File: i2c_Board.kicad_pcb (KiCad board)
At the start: 2 copper layers, 29.5 x 39.2 mm, 23 parts, among them J1 Conn_01x09_Pin, J2 Logic Analyzer Connector Pins, U1 MCP9808, U2 MCP7940N, Y1 Crystal

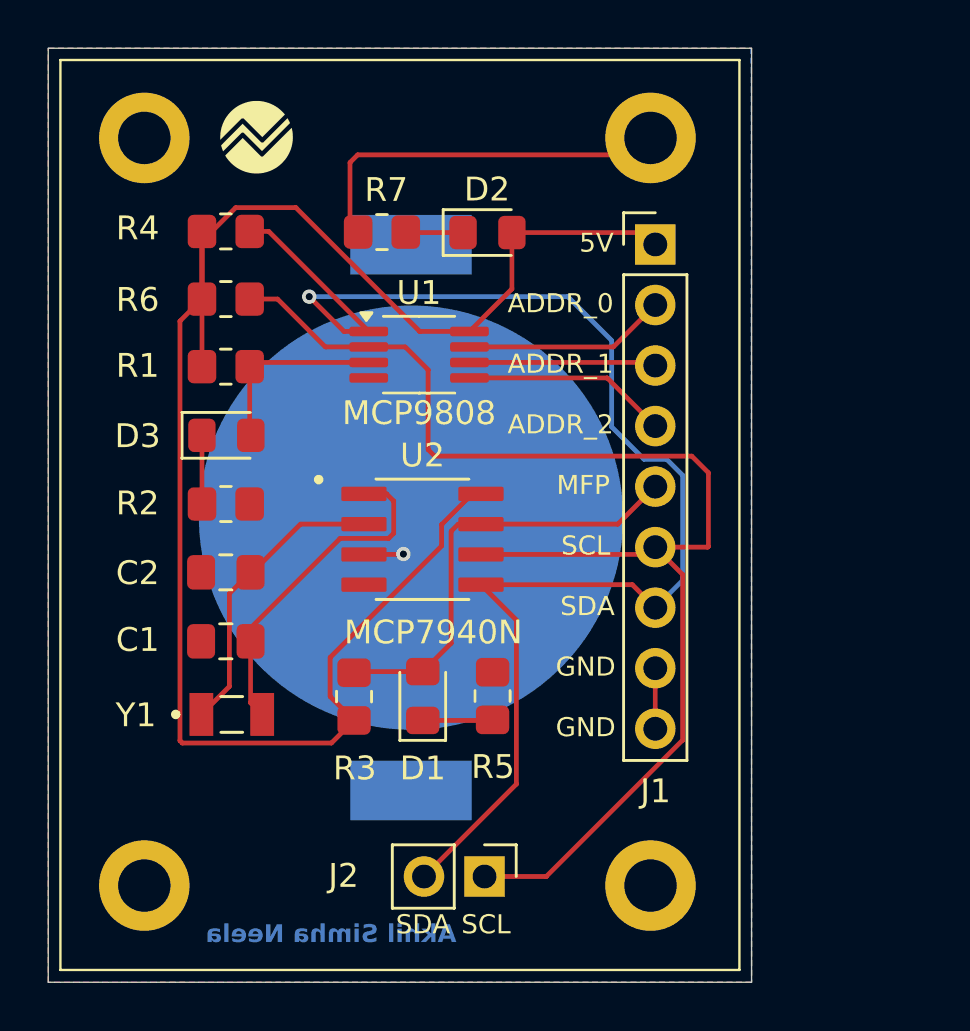
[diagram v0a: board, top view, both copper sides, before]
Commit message: Moved battery holder position
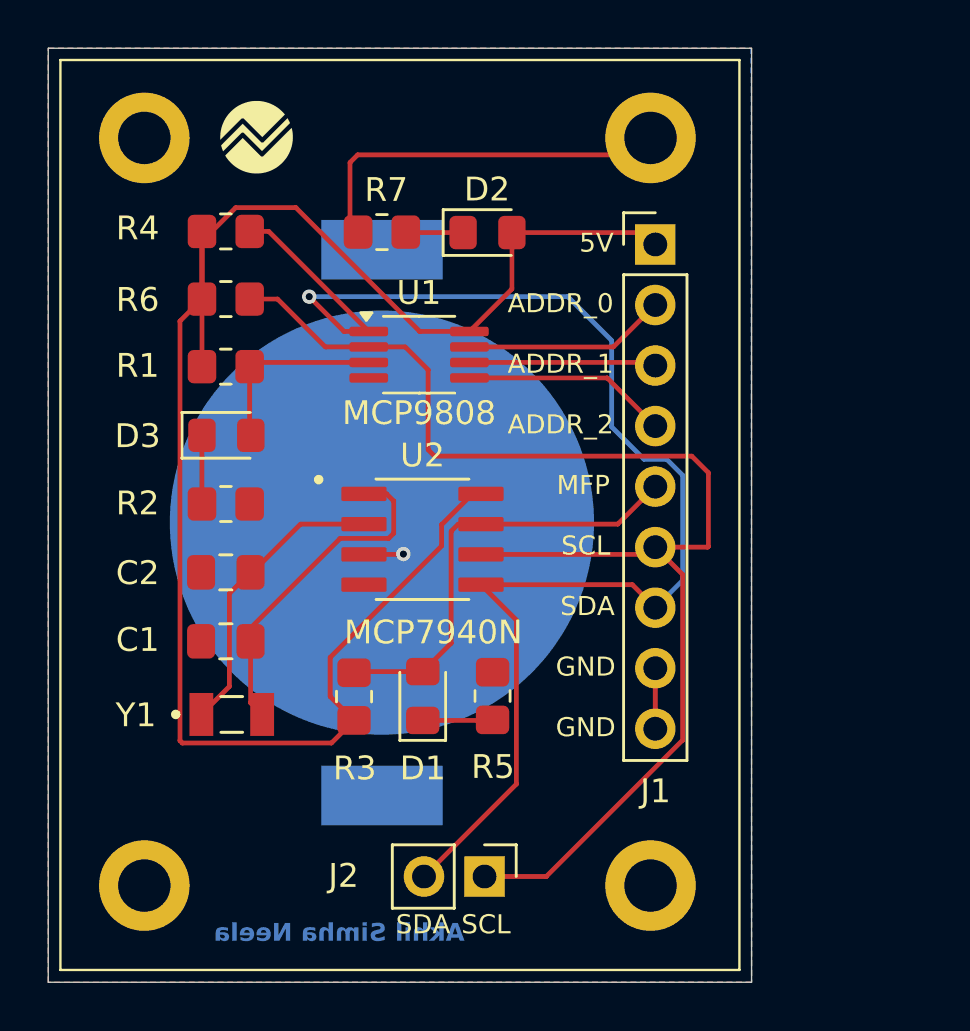
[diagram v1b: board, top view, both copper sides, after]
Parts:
- moved BT1 1.24 mm to (151.7, 92.1)
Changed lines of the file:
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@@
 	(footprint "BAT-HLD-002-SMT:BAT_BAT-HLD-002-SMT"
 		(layer "B.Cu")
-		(at 152.94 91.89 90)
+		(at 151.72 92.1 90)
 		(property "Reference" "BT1"
-			(at -11.82 -6.66 0)
+			(at 11.66 5.96 0)
 			(layer "B.SilkS")
 			(effects
@@
 	)
 	(gr_text "Akhil Simha Neela"
-		(at 154.85 109.79 -0)
+		(at 155.19 109.74 -0)
 		(layer "B.Cu")
 		(effects
@@
 	)
 	(gr_text "v 1.1"
-		(at 142.6 100.73 90)
+		(at 142.58 98.66 90)
 		(layer "B.SilkS")
 		(effects
 			(font
 				(size 1 1)
-				(thickness 0.2)
+				(thickness 0.125)
 				(bold yes)
 			)
@@
 	)
 	(gr_text "I2C Learning Board"
-		(at 142.59 78.16 90)
+		(at 141.09 80.58 90)
 		(layer "B.SilkS")
 		(effects

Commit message: Added Decoupling Capacitors
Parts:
- added C3: 0.1u, Capacitor_SMD:C_0805_2012Metric_Pad1.18x1.45mm_HandSolder, F.Cu at (159.1, 82.6)
- added C4: 0.1u, Capacitor_SMD:C_0805_2012Metric_Pad1.18x1.45mm_HandSolder, F.Cu at (159.6, 90.7)
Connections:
- U1 pad 8: +5V -> Net-(U1-V_{DD})
- U2 pad 8: +5V -> Net-(U2-VCC)
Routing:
- net GND: track 18.7 -> 45.8 mm, vias 0 -> 2
- net +5V: track 72.6 -> 81.3 mm
- net Net-(U1-V_{DD}): track 0.00 -> 3.89 mm
- net Net-(U2-VCC): track 0.00 -> 2.78 mm

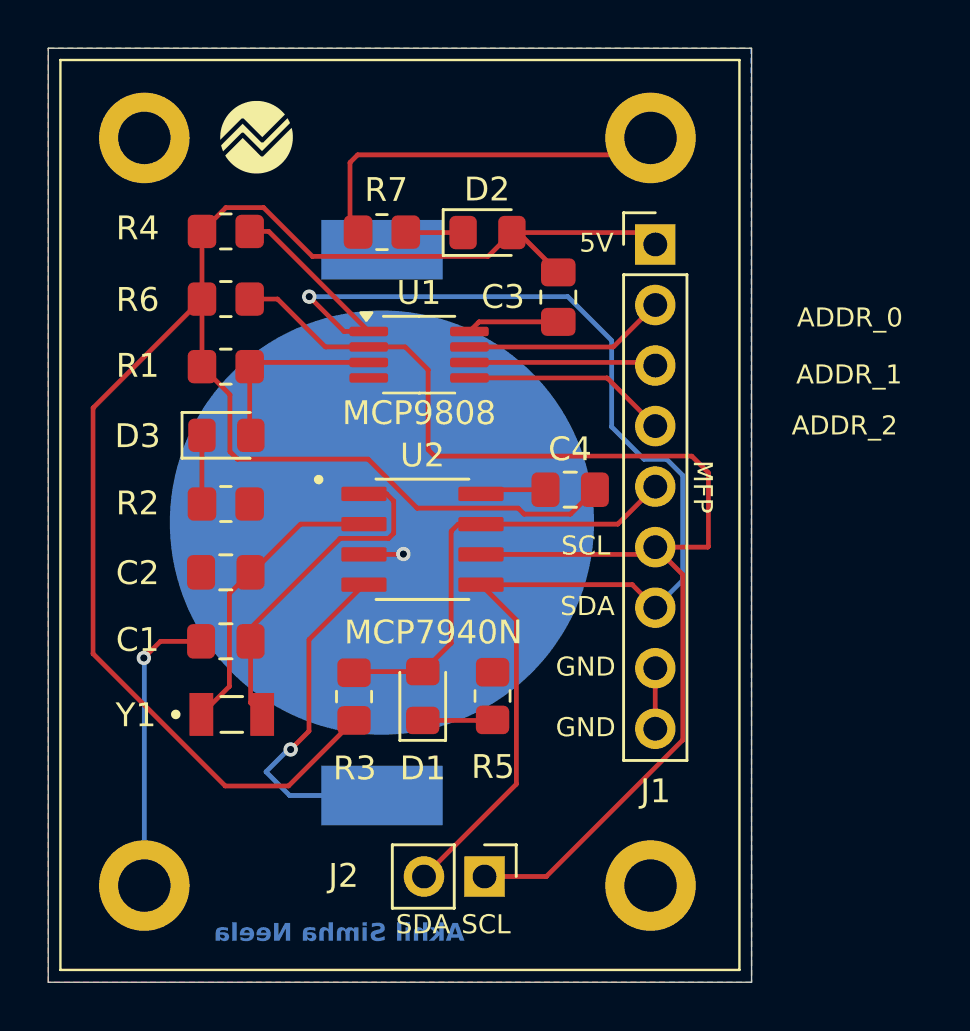
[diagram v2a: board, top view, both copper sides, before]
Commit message: Flipped incorrect battery polarity
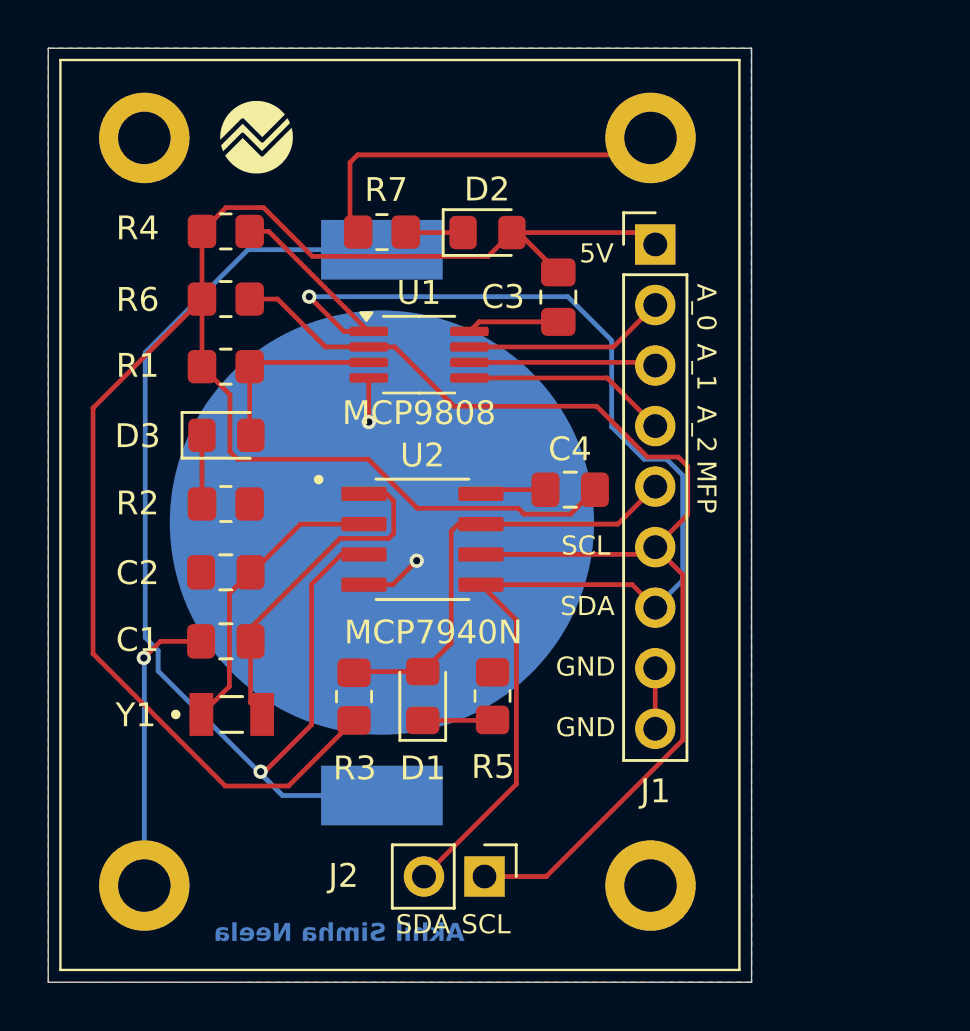
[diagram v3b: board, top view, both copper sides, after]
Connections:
- BT1 pad N: Net-(U2-VBAT) -> GND
- BT1 pad P1: GND -> Net-(U2-VBAT)
- BT1 pad P2: GND -> Net-(U2-VBAT)
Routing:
- net Net-(U2-VBAT): track 1.66 -> 49.8 mm
- net GND: track 45.8 -> 35.4 mm, vias 2 -> 3
- net MCU_SCL: track 56.3 -> 51.9 mm
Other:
- board text added: "A_0"
- board text added: "A_1"
- board text added: "A_2"
- board text removed: "ADDR_0"
- board text removed: "ADDR_1"
- board text removed: "ADDR_2"
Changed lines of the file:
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@@
 			(size 17.8 17.8)
 			(layers "B.Cu" "B.Mask")
-			(net 15 "Net-(U2-VBAT)")
+			(net 1 "GND")
 			(pintype "passive")
 			(solder_mask_margin 0.102)
@@
 			(size 2.5 5.1)
 			(layers "B.Cu" "B.Paste" "B.Mask")
-			(net 1 "GND")
+			(net 15 "Net-(U2-VBAT)")
 			(pintype "passive")
 			(solder_mask_margin 0.102)
@@
 			(size 2.5 5.1)
 			(layers "B.Cu" "B.Paste" "B.Mask")
-			(net 1 "GND")
+			(net 15 "Net-(U2-VBAT)")
 			(pintype "passive")
 			(solder_mask_margin 0.102)
@@
 		)
 	)
-	(gr_text "ADDR_0"
-		(at 169.13 83.97 0)
+	(gr_text "A_0"
+		(at 164.86 82.07 -90)
 		(layer "F.SilkS")
 		(effects
@@
 		)
 	)
-	(gr_text "ADDR_1"
-		(at 169.1 86.36 0)
+	(gr_text "A_1"
+		(at 164.86 84.58 -90)
 		(layer "F.SilkS")
 		(effects
@@
 	)
 	(gr_text "MFP"
-		(at 164.71 89.48 -90)
+		(at 164.86 89.48 -90)
 		(layer "F.SilkS")
 		(effects
@@
 	)
 	(gr_text "5V"
-		(at 160.000476 80.83 0)
+		(at 160.000476 81.28 0)
 		(layer "F.SilkS")
 		(effects
@@
 		)
 	)
-	(gr_text "ADDR_2"
-		(at 168.91 88.5 0)
+	(gr_text "A_2"
+		(at 164.86 87.18 -90)
 		(layer "F.SilkS")
 		(effects
@@
 	)
 	(segment
+		(start 152.175 94.705)
+		(end 153.18 93.7)
+		(width 0.2)
+		(layer "F.Cu")
+		(net 1)
+	)
+	(segment
+		(start 150.965 94.705)
+		(end 152.175 94.705)
+		(width 0.2)
+		(layer "F.Cu")
+		(net 1)
+	)
+	(segment
 		(start 141.73 97.78)
 		(end 142.427144 97.082856)
@@
 	)
 	(segment
+		(start 151.1675 86.03)
+		(end 151.1675 87.8775)
+		(width 0.2)
+		(layer "F.Cu")
+		(net 1)
+	)
+	(segment
 		(start 142.427144 97.082856)
 		(end 144.1325 97.082856)
@@
 	)
 	(segment
-		(start 148.66 100.85)
-		(end 148.66 97.01)
+		(start 151.1675 87.8775)
+		(end 151.17 87.88)
 		(width 0.2)
 		(layer "F.Cu")
@@
 		(net 1)
 	)
-	(segment
-		(start 148.66 97.01)
-		(end 150.965 94.705)
-		(width 0.2)
-		(layer "F.Cu")
-		(net 1)
-	)
-	(segment
-		(start 147.89 101.62)
-		(end 148.66 100.85)
-		(width 0.2)
-		(layer "F.Cu")
+	(via
+		(at 151.17 87.88)
+		(size 0.6)
+		(drill 0.3)
+		(layers "F.Cu" "B.Cu")
 		(net 1)
 	)
@@
 	)
 	(via
-		(at 147.89 101.62)
+		(at 153.18 93.7)
 		(size 0.6)
 		(drill 0.3)
@@
 	)
 	(segment
-		(start 147.89 101.62)
-		(end 147.79 101.62)
-		(width 0.2)
-		(layer "B.Cu")
-		(net 1)
-	)
-	(segment
 		(start 141.73 97.78)
 		(end 141.75 97.8)
@@
 	)
 	(segment
-		(start 146.86 102.56)
-		(end 147.85 103.55)
-		(width 0.2)
-		(layer "B.Cu")
-		(net 1)
-	)
-	(segment
-		(start 147.79 101.62)
-		(end 146.86 102.55)
-		(width 0.2)
-		(layer "B.Cu")
-		(net 1)
-	)
-	(segment
-		(start 147.85 103.55)
-		(end 151.72 103.55)
-		(width 0.2)
-		(layer "B.Cu")
-		(net 1)
-	)
-	(segment
-		(start 146.86 102.55)
-		(end 146.86 102.56)
-		(width 0.2)
-		(layer "B.Cu")
-		(net 1)
-	)
-	(segment
 		(start 152.215 92.54741)
 		(end 151.99741 92.765)
@@
 	)
 	(segment
+		(start 164.55 89.74)
+		(end 164.55 91.77)
+		(width 0.2)
+		(layer "F.Cu")
+		(net 11)
+	)
+	(segment
+		(start 151.1675 84.73)
+		(end 152.26 84.73)
+		(width 0.2)
+		(layer "F.Cu")
+		(net 11)
+	)
+	(segment
 		(start 163.19 93.13)
 		(end 164.34 94.28)
@@
 	)
 	(segment
-		(start 165.39 93.13)
-		(end 165.42 93.1)
+		(start 152.26 84.73)
+		(end 154.75 87.22)
 		(width 0.2)
 		(layer "F.Cu")
@@
 	)
 	(segment
-		(start 165.42 90.01)
-		(end 165.42 93.1)
-		(width 0.2)
-		(layer "F.Cu")
-		(net 11)
-	)
-	(segment
-		(start 153.93 89.31)
-		(end 164.72 89.31)
-		(width 0.2)
-		(layer "F.Cu")
-		(net 11)
-	)
-	(segment
-		(start 164.72 89.31)
-		(end 165.42 90.01)
-		(width 0.2)
-		(layer "F.Cu")
-		(net 11)
-	)
-	(segment
-		(start 153.66 85.69)
-		(end 153.66 89.04)
-		(width 0.2)
-		(layer "F.Cu")
-		(net 11)
-	)
-	(segment
 		(start 164.34 101.226346)
 		(end 158.616346 106.95)
@@
 	)
 	(segment
-		(start 153.66 89.04)
-		(end 153.93 89.31)
-		(width 0.2)
-		(layer "F.Cu")
-		(net 11)
-	)
-	(segment
 		(start 149.35 84.73)
 		(end 151.1675 84.73)
@@
 	)
 	(segment
-		(start 152.7 84.73)
-		(end 153.66 85.69)
-		(width 0.2)
-		(layer "F.Cu")
-		(net 11)
-	)
-	(segment
-		(start 151.1675 84.73)
-		(end 152.7 84.73)
+		(start 162.863654 89.35)
+		(end 164.16 89.35)
+		(width 0.2)
+		(layer "F.Cu")
+		(net 11)
+	)
+	(segment
+		(start 154.75 87.22)
+		(end 160.733654 87.22)
+		(width 0.2)
+		(layer "F.Cu")
+		(net 11)
+	)
+	(segment
+		(start 164.16 89.35)
+		(end 164.55 89.74)
 		(width 0.2)
 		(layer "F.Cu")
@@
 	)
 	(segment
-		(start 163.19 93.13)
-		(end 165.39 93.13)
+		(start 164.55 91.77)
+		(end 163.19 93.13)
 		(width 0.2)
 		(layer "F.Cu")
@@
 		(start 162.885 93.435)
 		(end 163.19 93.13)
+		(width 0.2)
+		(layer "F.Cu")
+		(net 11)
+	)
+	(segment
+		(start 160.733654 87.22)
+		(end 162.863654 89.35)
 		(width 0.2)
 		(layer "F.Cu")
@@
 	)
 	(segment
-		(start 152.62 93.42)
-		(end 152.605 93.435)
-		(width 0.2)
-		(layer "F.Cu")
-		(net 15)
-	)
-	(segment
-		(start 152.605 93.435)
+		(start 150.015001 93.435)
 		(end 150.965 93.435)
 		(width 0.2)
@@
 		(net 15)
 	)
+	(segment
+		(start 146.63 102.55)
+		(end 146.8 102.55)
+		(width 0.2)
+		(layer "F.Cu")
+		(net 15)
+	)
+	(segment
+		(start 148.77 94.680001)
+		(end 150.015001 93.435)
+		(width 0.2)
+		(layer "F.Cu")
+		(net 15)
+	)
+	(segment
+		(start 146.8 102.55)
+		(end 148.77 100.58)
+		(width 0.2)
+		(layer "F.Cu")
+		(net 15)
+	)
+	(segment
+		(start 148.77 100.58)
+		(end 148.77 94.680001)
+		(width 0.2)
+		(layer "F.Cu")
+		(net 15)
+	)
 	(via
-		(at 152.62 93.42)
+		(at 146.63 102.55)
 		(size 0.6)
 		(drill 0.3)
@@
 		(net 15)
 	)
+	(segment
+		(start 146.63 102.63)
+		(end 147.55 103.55)
+		(width 0.2)
+		(layer "B.Cu")
+		(net 15)
+	)
+	(segment
+		(start 141.79 84.96)
+		(end 141.79 96.93)
+		(width 0.2)
+		(layer "B.Cu")
+		(net 15)
+	)
+	(segment
+		(start 141.79 96.93)
+		(end 142.33 97.47)
+		(width 0.2)
+		(layer "B.Cu")
+		(net 15)
+	)
+	(segment
+		(start 146.63 102.55)
+		(end 146.63 102.63)
+		(width 0.2)
+		(layer "B.Cu")
+		(net 15)
+	)
+	(segment
+		(start 151.72 80.65)
+		(end 146.1 80.65)
+		(width 0.2)
+		(layer "B.Cu")
+		(net 15)
+	)
+	(segment
+		(start 142.33 98.33)
+		(end 147.55 103.55)
+		(width 0.2)
+		(layer "B.Cu")
+		(net 15)
+	)
+	(segment
+		(start 147.55 103.55)
+		(end 151.72 103.55)
+		(width 0.2)
+		(layer "B.Cu")
+		(net 15)
+	)
+	(segment
+		(start 142.33 97.47)
+		(end 142.33 98.33)
+		(width 0.2)
+		(layer "B.Cu")
+		(net 15)
+	)
+	(segment
+		(start 146.1 80.65)
+		(end 141.79 84.96)
+		(width 0.2)
+		(layer "B.Cu")
+		(net 15)
+	)
